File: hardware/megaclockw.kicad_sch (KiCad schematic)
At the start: 3 parts, among them J1 Conn_01x08_Female, U1 74HC245

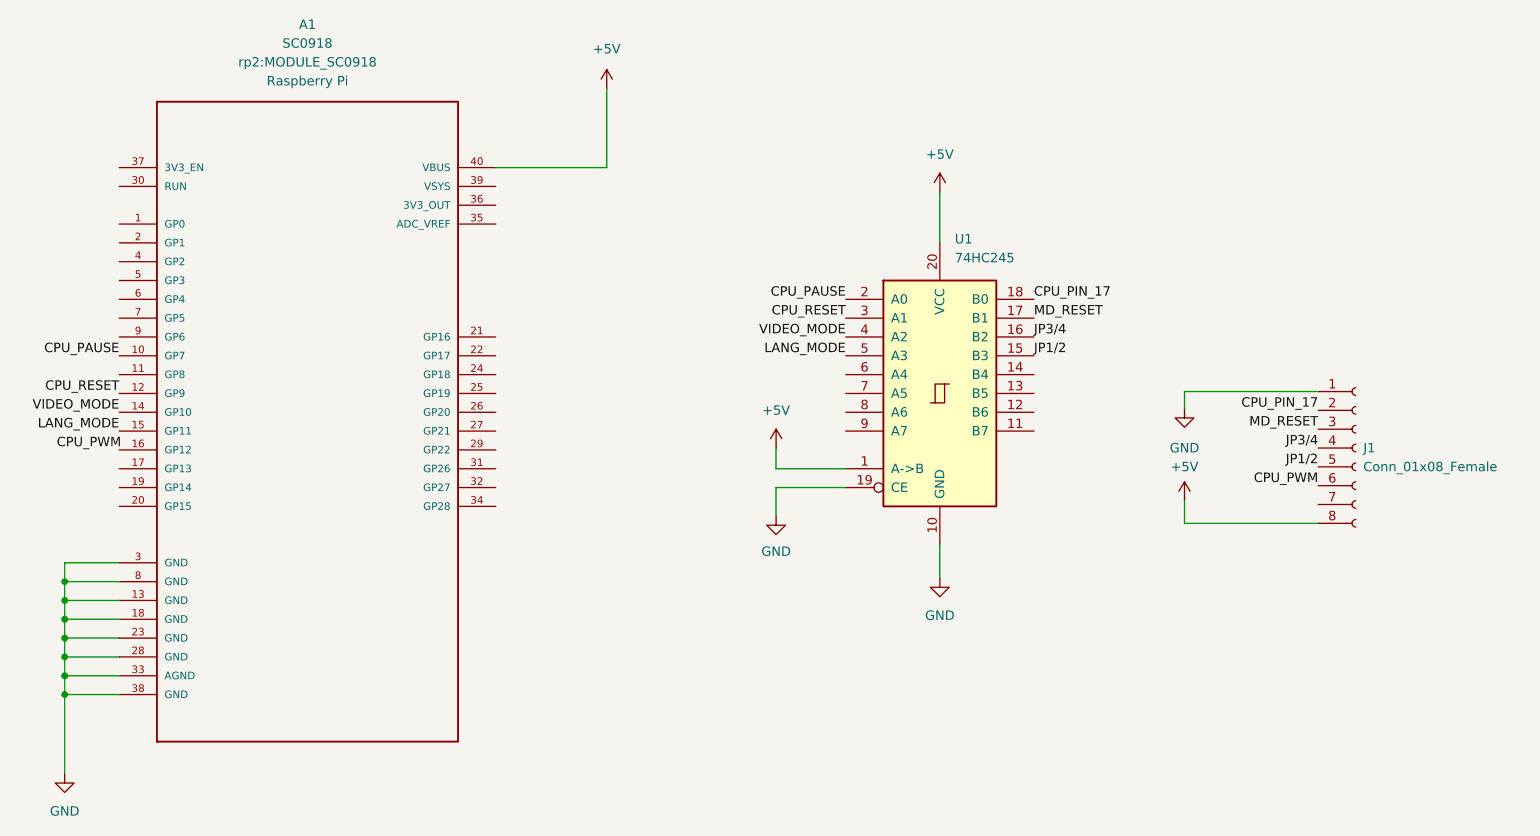
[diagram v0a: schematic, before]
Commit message: better power lines
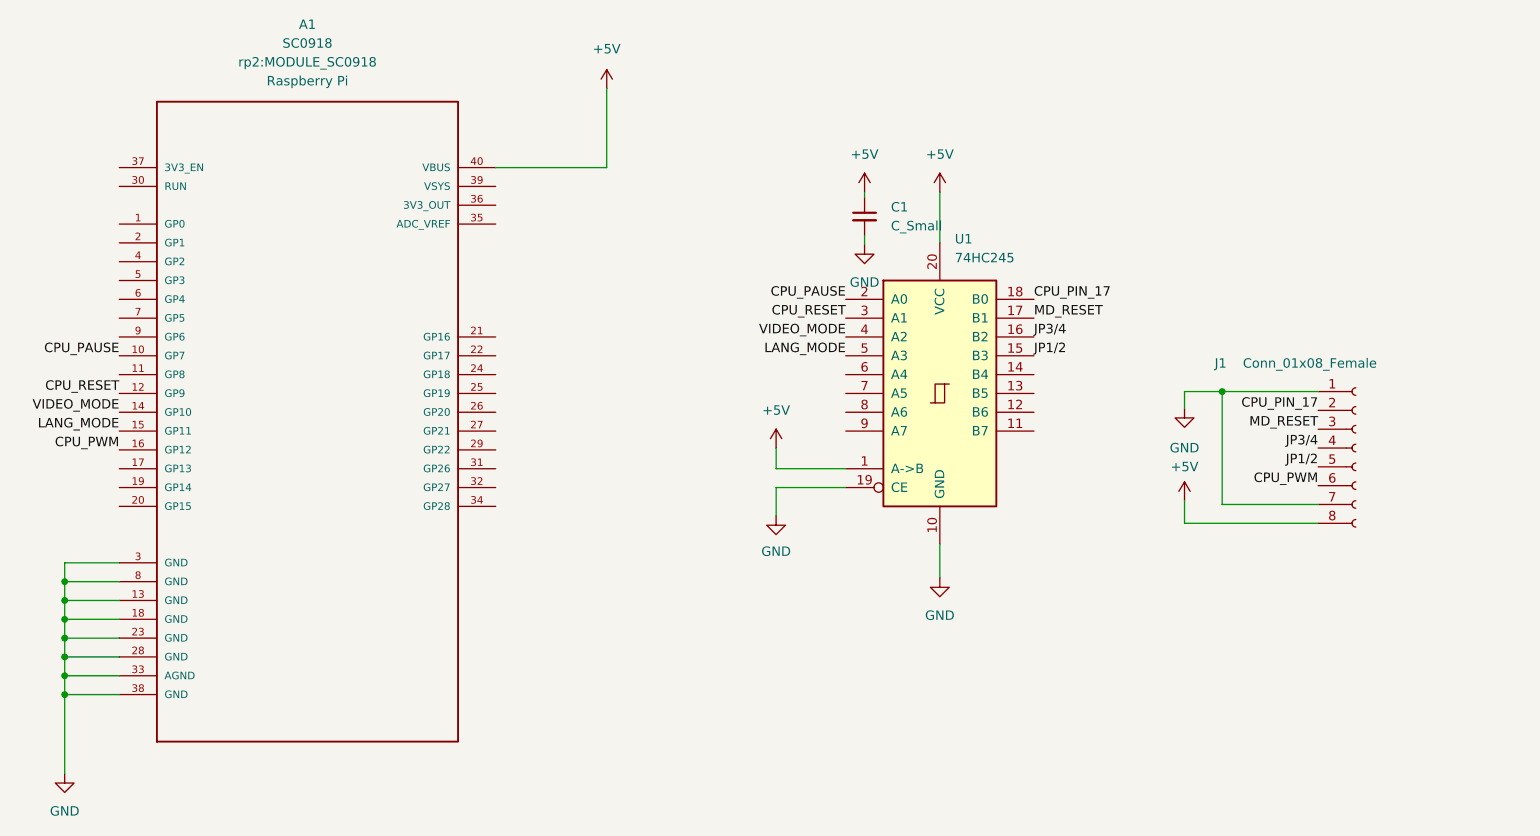
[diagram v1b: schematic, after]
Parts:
- added C1: C_Small, Capacitor_SMD:C_0603_1608Metric, symbol Device:C_Small
- U1: footprint Package_SO:SOP-20_7.5x12.8mm_P1.27mm -> Package_SO:SOIC-20W_7.5x12.8mm_P1.27mm
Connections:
- net +5V: now also C1.1
- net CPU_PWM: now also A1.16 (GP12)
- net GND: now also J1.7 (Pin_7), C1.2
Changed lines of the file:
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@@
   (junction (at 40.894 110.744) (diameter 0) (color 0 0 0 0)
   )
+  (junction (at 197.104 82.55) (diameter 0) (color 0 0 0 0)
+  )
   (wire (pts (xy 48.26 105.664) (xy 40.894 105.664))
     (stroke (width 0) (type default) (color 0 0 0 0))
@@
     (stroke (width 0) (type default) (color 0 0 0 0))
   )
+  (wire (pts (xy 148.844 61.468) (xy 148.844 62.738))
+    (stroke (width 0) (type default) (color 0 0 0 0))
+  )
   (wire (pts (xy 48.26 115.824) (xy 40.894 115.824))
     (stroke (width 0) (type default) (color 0 0 0 0))
@@
     (stroke (width 0) (type default) (color 0 0 0 0))
   )
+  (wire (pts (xy 197.104 97.79) (xy 197.104 82.55))
+    (stroke (width 0) (type default) (color 0 0 0 0))
+  )
   (wire (pts (xy 136.906 92.964) (xy 146.304 92.964))
     (stroke (width 0) (type default) (color 0 0 0 0))
   )
-  (wire (pts (xy 192.024 82.55) (xy 210.058 82.55))
+  (wire (pts (xy 197.104 82.55) (xy 210.058 82.55))
+    (stroke (width 0) (type default) (color 0 0 0 0))
+  )
+  (wire (pts (xy 192.024 82.55) (xy 197.104 82.55))
+    (stroke (width 0) (type default) (color 0 0 0 0))
+  )
+  (wire (pts (xy 148.844 55.626) (xy 148.844 56.388))
     (stroke (width 0) (type default) (color 0 0 0 0))
   )
@@
     (stroke (width 0) (type default) (color 0 0 0 0))
   )
+  (wire (pts (xy 210.058 97.79) (xy 197.104 97.79))
+    (stroke (width 0) (type default) (color 0 0 0 0))
+  )
   (wire (pts (xy 99.06 52.324) (xy 114.046 52.324))
     (stroke (width 0) (type default) (color 0 0 0 0))
@@
     (stroke (width 0) (type default) (color 0 0 0 0))
   )
-  (label "CPU_PWM" (at 48.514 90.424 180)
+  (label "CPU_PWM" (at 48.26 90.424 180)
     (effects (font (size 1.27 1.27)) (justify right bottom))
   )
   (label "CPU_PIN_17" (at 210.058 85.09 180)
+    (effects (font (size 1.27 1.27)) (justify right bottom))
+  )
+  (label "CPU_PWM" (at 210.058 95.25 180)
     (effects (font (size 1.27 1.27)) (justify right bottom))
   )
@@
     (effects (font (size 1.27 1.27)) (justify right bottom))
   )
-  (label "CPU_PWM" (at 210.058 95.25 180)
-    (effects (font (size 1.27 1.27)) (justify right bottom))
-  )
   (label "LANG_MODE" (at 48.26 87.884 180)
     (effects (font (size 1.27 1.27)) (justify right bottom))
@@
     )
     (pin "1")
+  )
+  (symbol (lib_id "Device:C_Small") (at 148.844 58.928 0) (unit 1)
+    (in_bom yes) (on_board yes) (fields_autoplaced)
+    (property "Reference" "C1" (id 0) (at 152.4 57.6642 0)
+      (effects (font (size 1.27 1.27)) (justify left))
+    )
+    (property "Value" "C_Small" (id 1) (at 152.4 60.2042 0)
+      (effects (font (size 1.27 1.27)) (justify left))
+    )
+    (property "Footprint" "Capacitor_SMD:C_0603_1608Metric" (id 2) (at 148.844 58.928 0)
+      (effects (font (size 1.27 1.27)) hide)
+    )
+    (property "Datasheet" "~" (id 3) (at 148.844 58.928 0)
+      (effects (font (size 1.27 1.27)) hide)
+    )
+    (pin "1")
+    (pin "2")
   )
   (symbol (lib_id "rp2:SC0918") (at 73.66 86.614 0) (unit 1)
@@
     (pin "1")
   )
+  (symbol (lib_id "power:GND") (at 148.844 62.738 0) (unit 1)
+    (in_bom yes) (on_board yes) (fields_autoplaced)
+    (property "Reference" "#PWR0110" (id 0) (at 148.844 69.088 0)
+      (effects (font (size 1.27 1.27)) hide)
+    )
+    (property "Value" "GND" (id 1) (at 148.844 67.818 0))
+    (property "Footprint" "" (id 2) (at 148.844 62.738 0)
+      (effects (font (size 1.27 1.27)) hide)
+    )
+    (property "Datasheet" "" (id 3) (at 148.844 62.738 0)
+      (effects (font (size 1.27 1.27)) hide)
+    )
+    (pin "1")
+  )
   (symbol (lib_id "power:GND") (at 159.004 107.696 0) (unit 1)
     (in_bom yes) (on_board yes) (fields_autoplaced)
@@
     (pin "1")
   )
+  (symbol (lib_id "power:+5V") (at 148.844 55.626 0) (unit 1)
+    (in_bom yes) (on_board yes) (fields_autoplaced)
+    (property "Reference" "#PWR0109" (id 0) (at 148.844 59.436 0)
+      (effects (font (size 1.27 1.27)) hide)
+    )
+    (property "Value" "+5V" (id 1) (at 148.844 50.546 0))
+    (property "Footprint" "" (id 2) (at 148.844 55.626 0)
+      (effects (font (size 1.27 1.27)) hide)
+    )
+    (property "Datasheet" "" (id 3) (at 148.844 55.626 0)
+      (effects (font (size 1.27 1.27)) hide)
+    )
+    (pin "1")
+  )
   (symbol (lib_id "74xx:74HC245") (at 159.004 82.804 0) (unit 1)
     (in_bom yes) (on_board yes) (fields_autoplaced)
@@
       (effects (font (size 1.27 1.27)) (justify left))
     )
-    (property "Footprint" "Package_SO:SOP-20_7.5x12.8mm_P1.27mm" (id 2) (at 159.004 82.804 0)
+    (property "Footprint" "Package_SO:SOIC-20W_7.5x12.8mm_P1.27mm" (id 2) (at 159.004 82.804 0)
       (effects (font (size 1.27 1.27)) hide)
     )
@@
   )
   (symbol (lib_id "Connector:Conn_01x08_Female") (at 215.138 90.17 0) (unit 1)
-    (in_bom yes) (on_board yes) (fields_autoplaced)
-    (property "Reference" "J1" (id 0) (at 216.154 90.1699 0)
-      (effects (font (size 1.27 1.27)) (justify left))
-    )
-    (property "Value" "Conn_01x08_Female" (id 1) (at 216.154 92.7099 0)
+    (in_bom yes) (on_board yes)
+    (property "Reference" "J1" (id 0) (at 196.088 78.74 0)
+      (effects (font (size 1.27 1.27)) (justify left))
+    )
+    (property "Value" "Conn_01x08_Female" (id 1) (at 199.898 78.74 0)
       (effects (font (size 1.27 1.27)) (justify left))
     )
@@
       (reference "#PWR0108") (unit 1) (value "+5V") (footprint "")
     )
+    (path "/569642aa-f2be-4488-ab28-93d473e6723e"
+      (reference "#PWR0109") (unit 1) (value "+5V") (footprint "")
+    )
+    (path "/500d7f63-f15a-4a14-97b0-51b3bf4ad701"
+      (reference "#PWR0110") (unit 1) (value "GND") (footprint "")
+    )
     (path "/0ded6347-fba2-4ce2-bc6d-708d4bbcb684"
       (reference "A1") (unit 1) (value "SC0918") (footprint "rp2:MODULE_SC0918")
     )
+    (path "/099fc363-7ca3-443e-b5f6-b1e1d3f602bf"
+      (reference "C1") (unit 1) (value "C_Small") (footprint "Capacitor_SMD:C_0603_1608Metric")
+    )
     (path "/99cfac26-ca7d-4ef3-8296-bf1cb7785578"
       (reference "J1") (unit 1) (value "Conn_01x08_Female") (footprint "Connector_PinSocket_2.54mm:PinSocket_1x08_P2.54mm_Vertical")
     )
     (path "/6a3b2773-f8b1-490f-a446-8e77fc2bc296"
-      (reference "U1") (unit 1) (value "74HC245") (footprint "Package_SO:SOP-20_7.5x12.8mm_P1.27mm")
-    )
-  )
+      (reference "U1") (unit 1) (value "74HC245") (footprint "Package_SO:SOIC-20W_7.5x12.8mm_P1.27mm")
+    )
+  )
